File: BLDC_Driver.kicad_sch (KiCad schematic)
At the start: 54 parts, among them J4 Conn_01x03_Female, Q17 2N7000, Q18 IRF3205, Q19 IRF3205, Q20 IRF3205, Q21 IRF3205, Q22 IRF3205, Q23 IRF3205, Q24 IRF3205, Q25 2N7000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

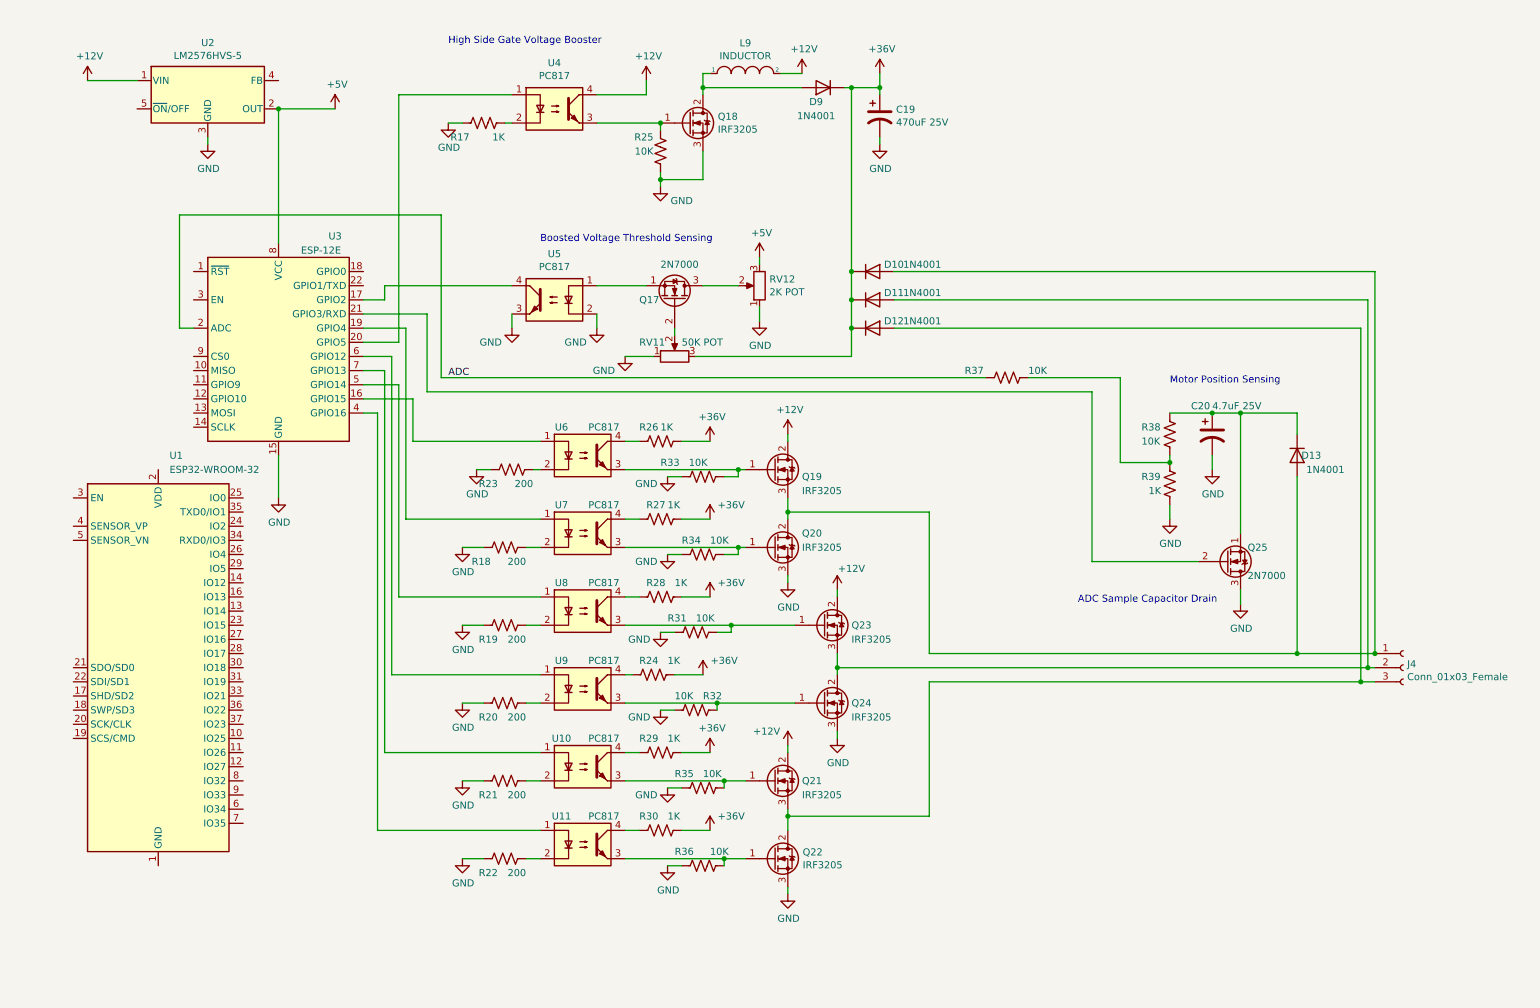
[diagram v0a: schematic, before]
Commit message: linked models so spice simulation runs
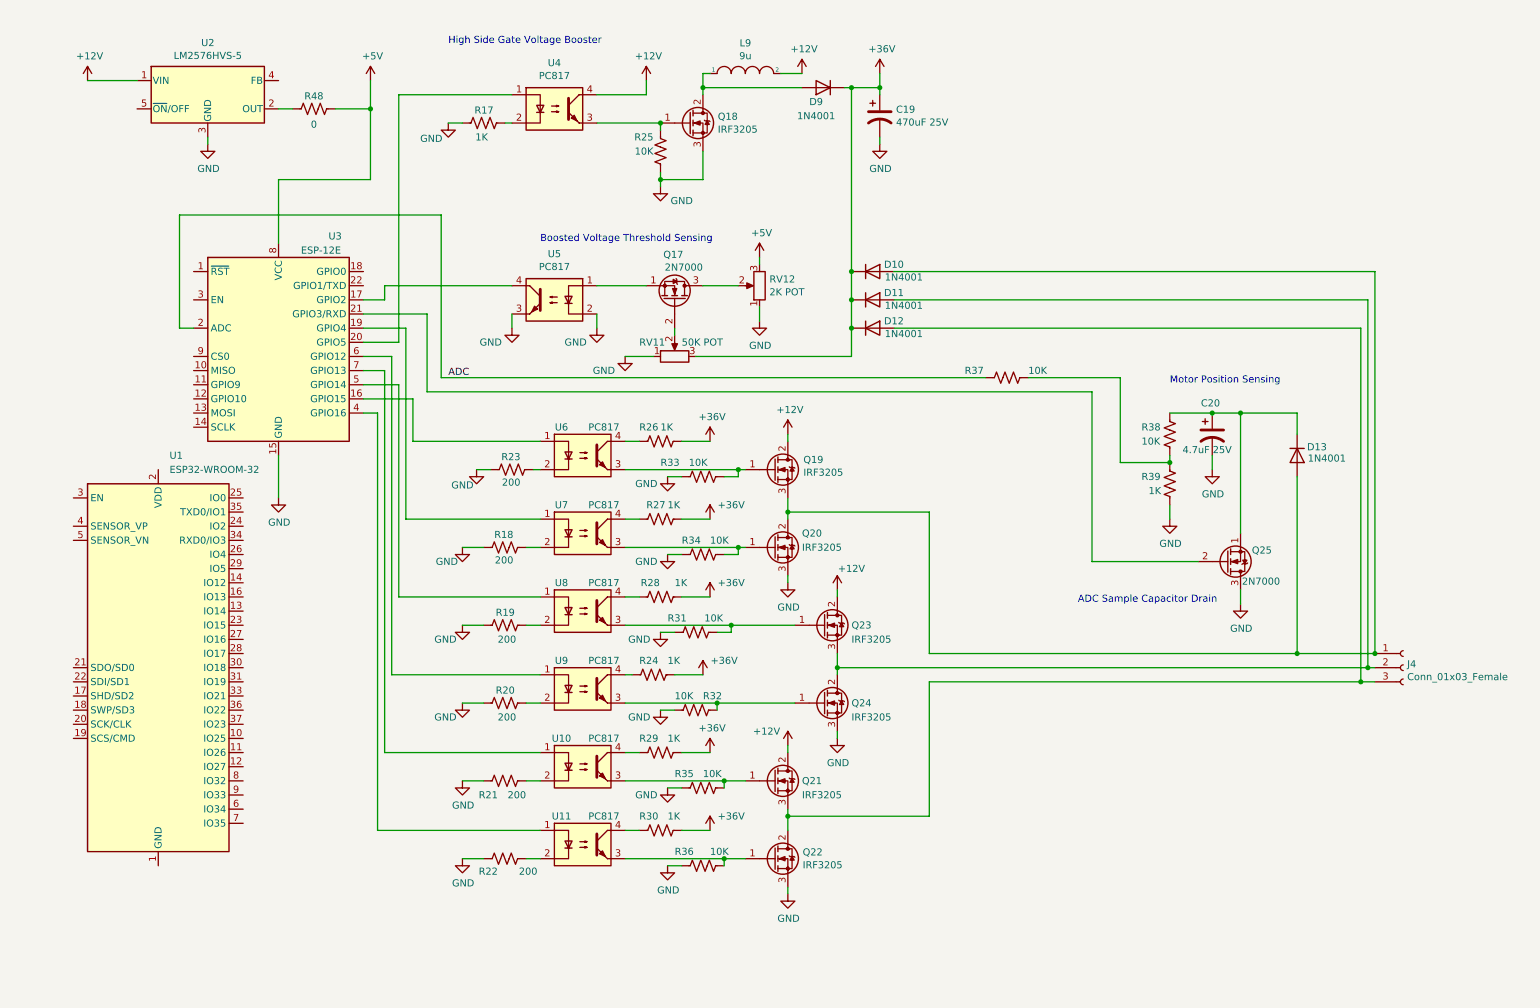
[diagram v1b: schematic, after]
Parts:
- added R48: 0, symbol Device:R_US
- L9: value INDUCTOR -> 9u
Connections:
- net +5V: now also R48.2; no longer U2.2 (OUT)
- new net: R48.1, U2.2 (OUT)

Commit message: added new spice directives to improve simulation speed, added sections for motor drivers, micro controlers, i2c bus connections, realized that focusing coils, hv, horizontal and vertical ramp will need time stable signals (not voltage dependant like with a voltage controlled oscilator) so it will be much simpler to design them with micro controllers
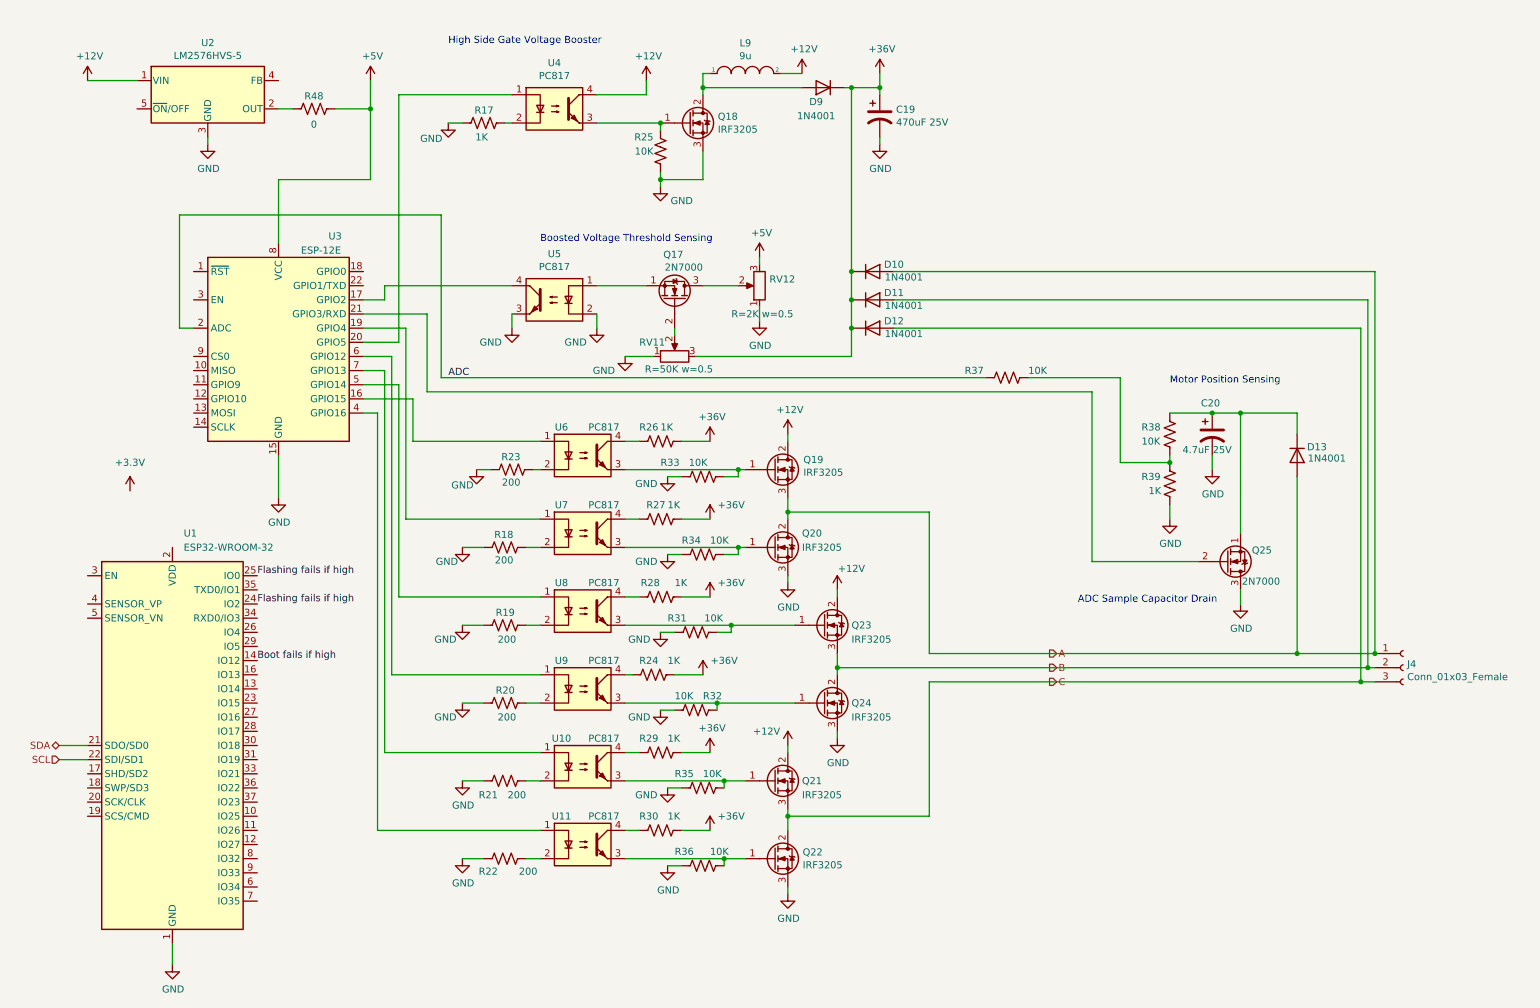
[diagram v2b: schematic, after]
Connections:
- net GND: now also U1.1 (GND), U1.15 (GND), U1.38 (GND), U1.39 (GND)
- net Boot fails if high: now reaches U1.14 (IO12)
- net SDA: now reaches U1.21 (SDO/SD0)
- net SCL: now reaches U1.22 (SDI/SD1)
- net Flashing fails if high: now reaches U1.24 (IO2)
- net Flashing fails if high: now also U1.25 (IO0)
- net A: now reaches D10.2 (A), D13.2 (A), J4.1 (Pin_1), Q19.3 (S), Q20.2 (D)
- net B: now reaches D11.2 (A), J4.2 (Pin_2), Q23.3 (S), Q24.2 (D)
- net C: now reaches D12.2 (A), J4.3 (Pin_3), Q21.3 (S), Q22.2 (D)
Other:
- moved on the sheet: U1

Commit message: changed bldc driver schematic to use esp32 devkit
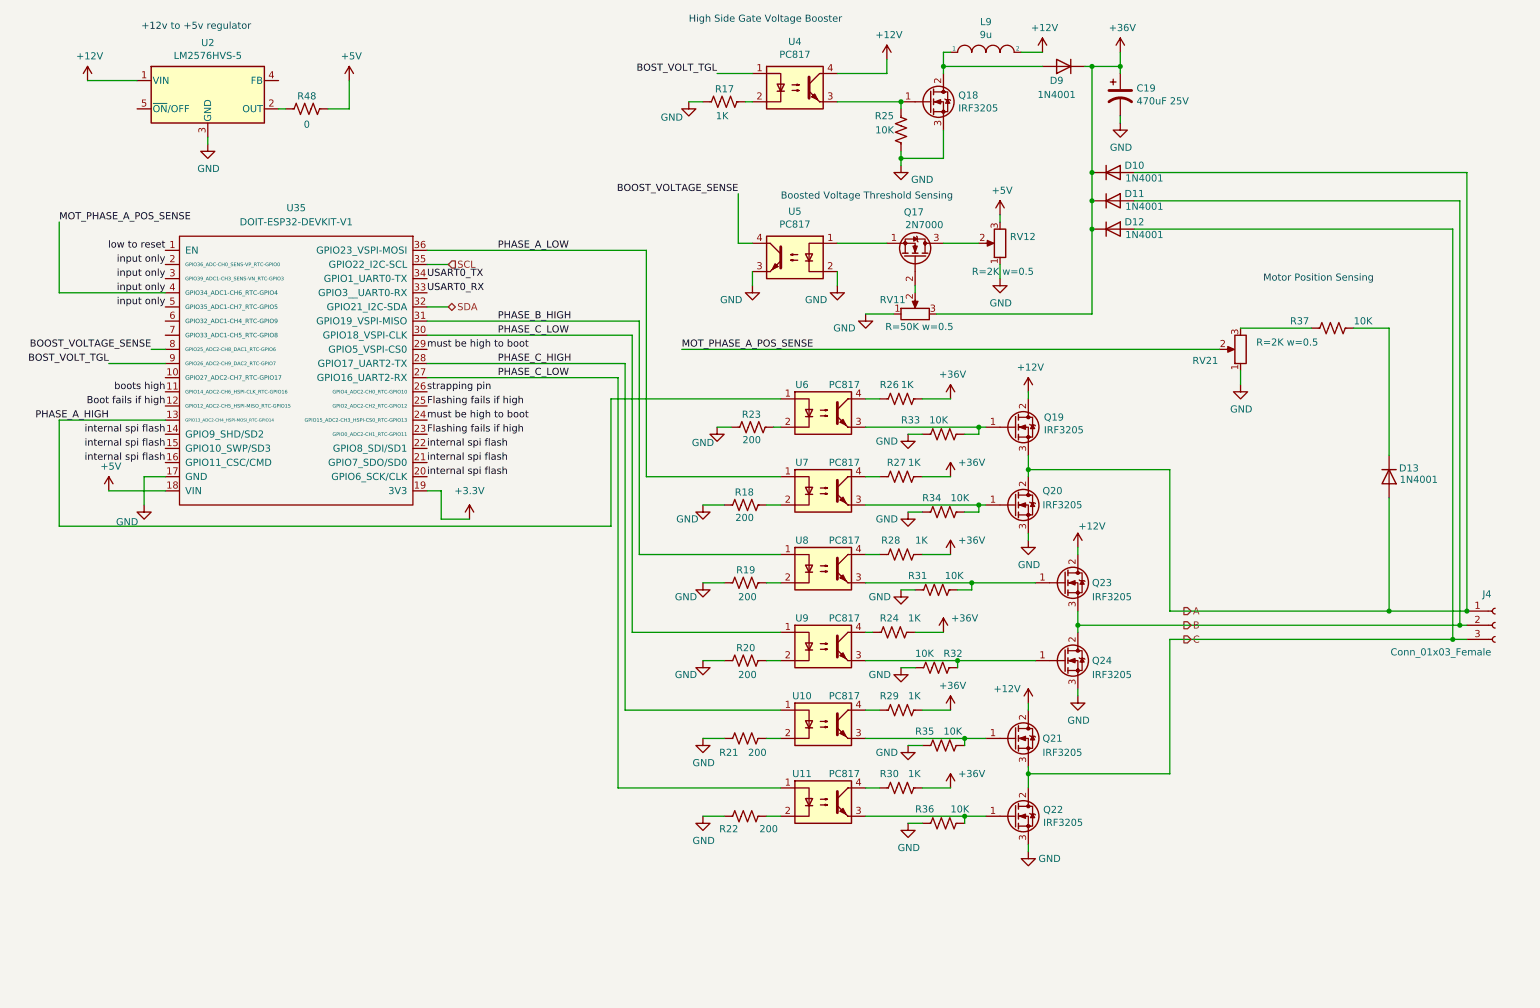
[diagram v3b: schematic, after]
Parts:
- removed C20: 4.7uF 25V, Capacitor_SMD:C_0603_1608Metric, symbol Device:CP1
- removed Q25: 2N7000, Package_TO_SOT_THT:TO-92_Inline, symbol Transistor_FET:2N7000
- removed R38: 10K, Resistor_SMD:R_0603_1608Metric, symbol Device:R_US
- removed R39: 1K, Resistor_SMD:R_0603_1608Metric, symbol Device:R_US
- removed U1: ESP32-WROOM-32, RF_Module:ESP32-WROOM-32, symbol RF_Module:ESP32-WROOM-32
- removed U3: ESP-12E, RF_Module:ESP-12E, symbol RF_Module:ESP-12E
- added RV21: 2K POT, Potentiometer_SMD:Potentiometer_ACP_CA6-VSMD_Vertical, symbol Device:R_POT
- added U35: DOIT-ESP32-DEVKIT-V1, crtDriver:ESP32-DOIT-DEVKIT, symbol doit-esp32-devkit-v1:DOIT-ESP32-DEVKIT-V1
- R48: footprint (none) -> Resistor_SMD:R_0603_1608Metric
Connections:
- net +3.3V: now also U35.19 (3V3)
- net +5V: now also U35.18 (VIN)
- net Boot fails if high: now also U35.12 (GPIO12_ADC2-CH5_HSPI-MISO_RTC-GPIO15)
- net Flashing fails if high: now also U35.23 (GPIO0_ADC2-CH1_RTC-GPIO11), U35.25 (GPIO2_ADC2-CH2_RTC-GPIO12)
- net GND: now also RV21.1, U35.17 (GND)
- net SCL: now also U35.35 (GPIO22_I2C-SCL)
- net SDA: now also U35.32 (GPIO21_I2C-SDA)
- net at D13.1 (K): now also R37.1
- net PHASE_A_HIGH: now reaches U6.1
- net PHASE_A_HIGH: now also U35.13 (GPIO13_ADC2-CH4_HSPI-MOSI_RTC-GPIO14)
- net BOOST_VOLTAGE_SENSE: now reaches U5.4
- net BOOST_VOLTAGE_SENSE: now also U35.8 (GPIO25_ADC2-CH8_DAC1_RTC-GPIO6)
- net PHASE_A_LOW: now reaches U7.1
- net PHASE_A_LOW: now also U35.36 (GPIO23_VSPI-MOSI)
- net BOST_VOLT_TGL: now reaches U4.1
- net BOST_VOLT_TGL: now also U35.9 (GPIO26_ADC2-CH9_DAC2_RTC-GPIO7)
- net PHASE_C_LOW: now reaches U11.1
- net PHASE_C_LOW: now also U9.1, U35.27 (GPIO16_UART2-RX), U35.30 (GPIO18_VSPI-CLK)
- net PHASE_B_HIGH: now reaches U8.1
- net PHASE_B_HIGH: now also U35.31 (GPIO19_VSPI-MISO)
- net PHASE_C_HIGH: now reaches U10.1
- net PHASE_C_HIGH: now also U35.28 (GPIO17_UART2-TX)
- net ADC: no longer names the net of R37.2
- net ADC: now also RV21.3
- new net MOT_PHASE_A_POS_SENSE: RV21.2, U35.2 (GPIO36_ADC-CH0_SENS-VP_RTC-GPIO0), U35.3 (GPIO39_ADC1-CH3_SENS-VN_RTC-GPIO3), U35.4 (GPIO34_ADC1-CH6_RTC-GPIO4), U35.5 (GPIO35_ADC1-CH7_RTC-GPIO5)
- new net USART0_RX: U35.33 (GPIO3__UART0-RX)
- new net USART0_TX: U35.34 (GPIO1_UART0-TX)
- new net boots high: U35.11 (GPIO14_ADC2-CH6_HSPI-CLK_RTC-GPIO16)
- new net internal spi flash: U35.14 (GPIO9_SHD/SD2), U35.15 (GPIO10_SWP/SD3), U35.16 (GPIO11_CSC/CMD), U35.20 (GPIO6_SCK/CLK), U35.21 (GPIO7_SDO/SD0), U35.22 (GPIO8_SDI/SD1)
- new net low to reset: U35.1 (EN)
- new net must be high to boot: U35.24 (GPIO15_ADC2-CH3_HSPI-CS0_RTC-GPIO13), U35.29 (GPIO5_VSPI-CS0)
- new net strapping pin: U35.26 (GPIO4_ADC2-CH0_RTC-GPIO10)
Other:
- note added: "+12v to +5v regulator"
- note removed: "ADC Sample Capacitor Drain"
- moved on the sheet: C19, D10, D11, D12, D13, D9, J4, L9, Q17, Q18, Q19, Q20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

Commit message: added sections to add to overview schematic, added some of the component schematics
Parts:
- added D32, D35, D38, D39, D44, D45: 1N4001, Diode_SMD:D_0805_2012Metric, symbol Device:D
- added R102, R105, R69, R94, R99: 10K, Resistor_SMD:R_0603_1608Metric, symbol Device:R_US
- added RV24, RV27: 2K POT, Potentiometer_SMD:Potentiometer_ACP_CA6-VSMD_Vertical, symbol Device:R_POT
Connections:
- net +3.3V: now also D32.2 (A), D38.2 (A), D44.2 (A)
- net B: now also R69.1
- net C: now also R94.1
- net GND: now also D35.2 (A), D39.2 (A), D45.2 (A), RV24.1, RV27.1
- net MOT_PHASE_A_POS_SENSE: now also R102.2, R105.2, R99.2; no longer RV21.2
- new net: D44.1 (K), D45.1 (K), R105.1, RV27.2
- new net: D38.1 (K), D39.1 (K), R102.1, RV24.2
- new net: D32.1 (K), D35.1 (K), R99.1, RV21.2
- new net: R69.2, RV24.3
- new net: R94.2, RV27.3
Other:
- moved on the sheet: D13
